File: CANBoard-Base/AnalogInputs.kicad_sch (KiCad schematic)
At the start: 26 parts, among them U2 LM324, U3 LM324, U4 SRV05-4

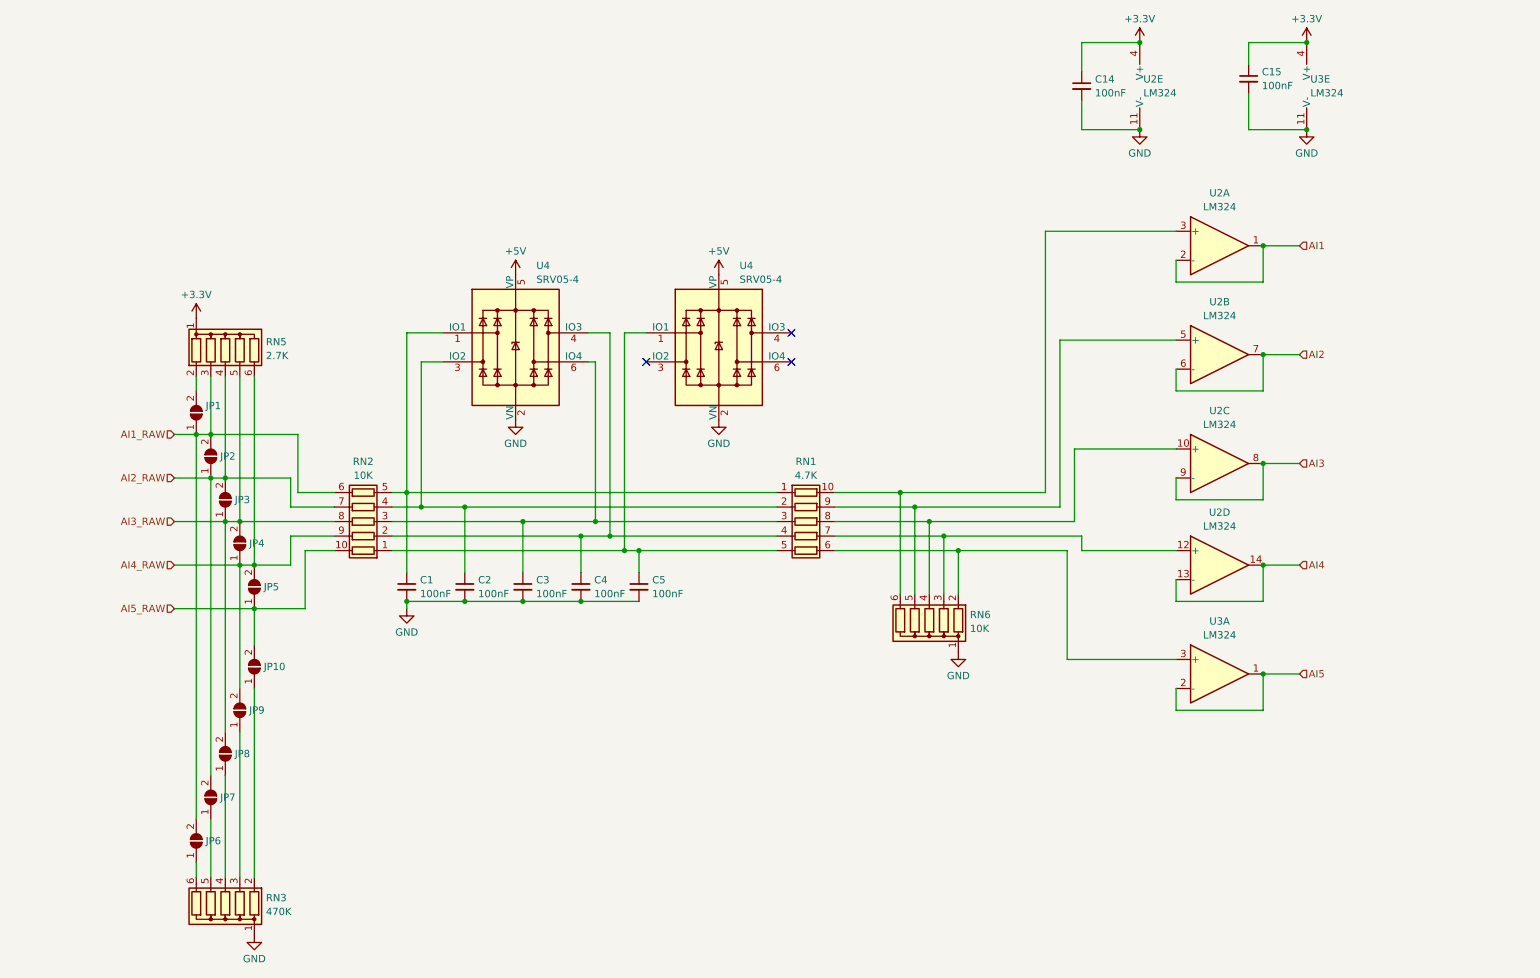
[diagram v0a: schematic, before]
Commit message: Switched to v2
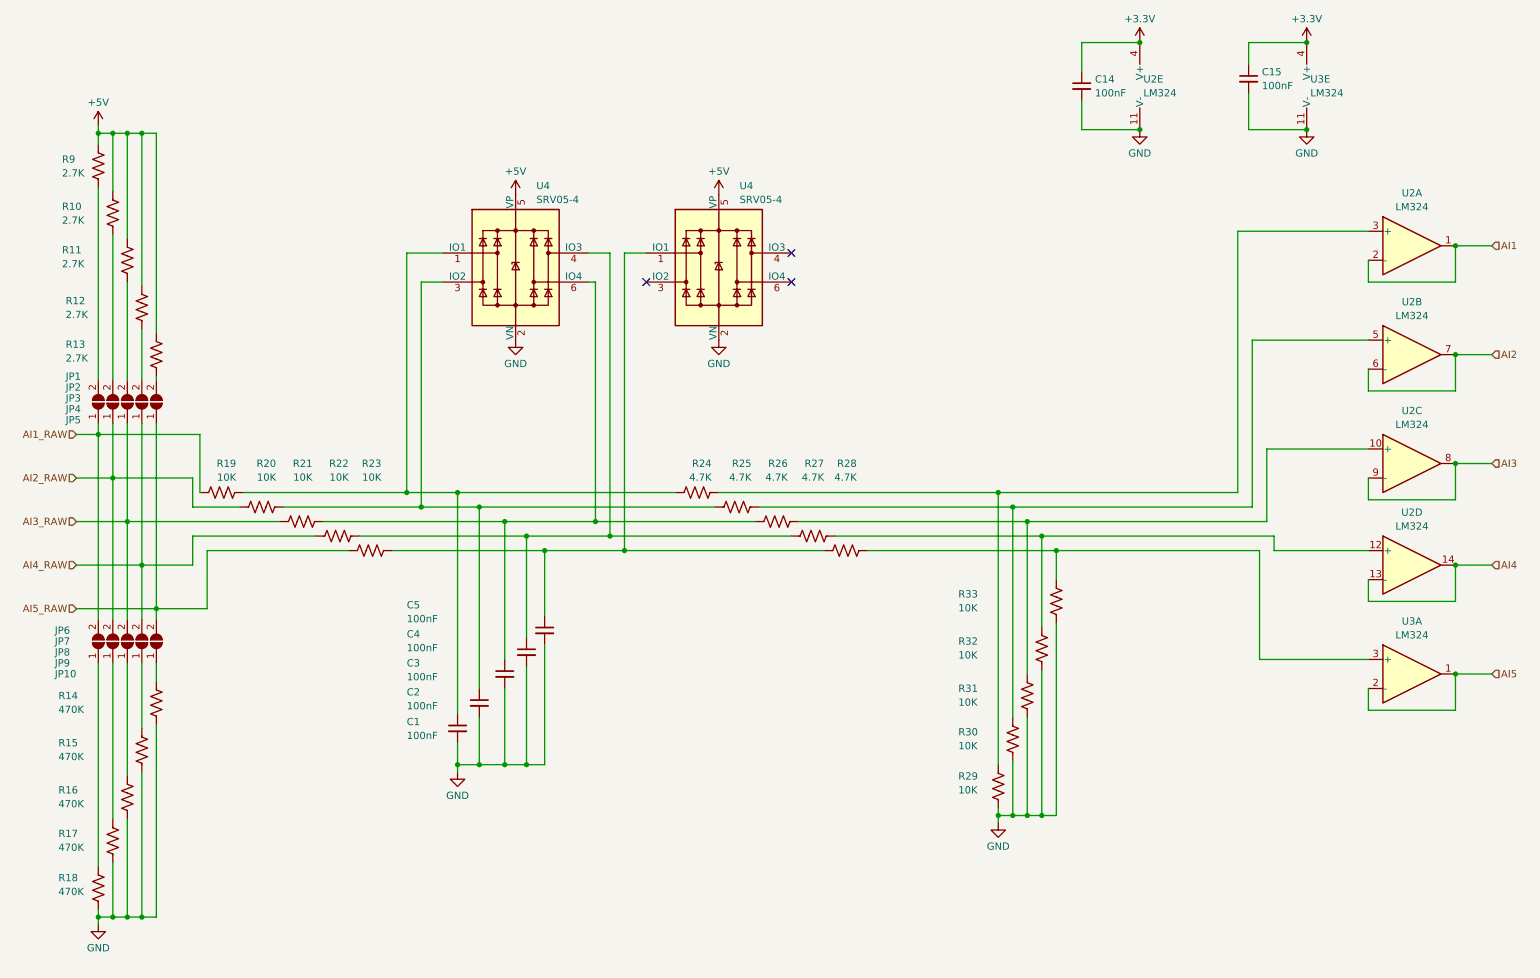
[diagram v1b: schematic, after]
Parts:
- removed RN1: 4.7K, symbol Device:R_Pack05
- removed RN2: 10K, symbol Device:R_Pack05
- removed RN3: 470K, Resistor_THT:R_Array_SIP6, symbol Device:R_Network05
- removed RN5: 2.7K, Resistor_THT:R_Array_SIP6, symbol Device:R_Network05
- removed RN6: 10K, Resistor_THT:R_Array_SIP6, symbol Device:R_Network05
- added R10, R11, R12, R13, R9: 2.7K, Resistor_SMD:R_0805_2012Metric, symbol Device:R_US
- added R14, R15, R16, R17, R18: 470K, Resistor_SMD:R_0805_2012Metric, symbol Device:R_US
- added R19, R20, R21, R22, R23, R29, R30, R31, R32, R33: 10K, Resistor_SMD:R_0805_2012Metric, symbol Device:R_US
- added R24, R25, R26, R27, R28: 4.7K, Resistor_SMD:R_0805_2012Metric, symbol Device:R_US
- JP1, JP10, JP2, JP3, JP4, JP5, JP6, JP7, JP8, JP9: footprint (none) -> Jumper:SolderJumper-2_P1.3mm_Open_RoundedPad1.0x1.5mm
- U2, U3: footprint (none) -> Package_SO:TSSOP-14_4.4x5mm_P0.65mm
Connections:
- net +5V: now also R10.1, R11.1, R12.1, R13.1, R9.1
- net AI1_RAW: now also R19.1; no longer JP2.2 (B)
- net AI2_RAW: now also R20.1; no longer JP3.2 (B)
- net AI3_RAW: now also R21.1; no longer JP4.2 (B)
- net AI4_RAW: now also R22.1; no longer JP5.2 (B)
- net AI5_RAW: now also R23.1
- net GND: now also R14.2, R15.2, R16.2, R17.2, R18.2, R29.2, R30.2, R31.2, R32.2, R33.2
- net at JP8.1 (A): now also R16.1
- net at JP9.1 (A): now also R15.1
- net at U2.10 (+): now also R26.2, R31.1
- net at JP1.2 (B): now also R9.2
- net at JP10.1 (A): now also R14.1
- net at JP7.1 (A): now also R17.1
- net at JP6.1 (A): now also R18.1
- net at C3.1, U4.6 (IO4): now also R21.2, R26.1
- net at U2.5 (+): now also R25.2, R30.1
- net at C1.1, U4.1 (IO1): now also R19.2, R24.1
- net at C2.1, U4.3 (IO2): now also R20.2, R25.1
- net at C4.1, U4.4 (IO3): now also R22.2, R27.1
- net at C5.1, U4.1 (IO1): now also R23.2, R28.1
- net at U2.3 (+): now also R24.2, R29.1
- net at U3.3 (+): now also R28.2, R33.1
- net at U2.12 (+): now also R27.2, R32.1
- new net: JP4.2 (B), R12.2
- new net: JP5.2 (B), R13.2
- new net: JP2.2 (B), R10.2
- new net: JP3.2 (B), R11.2
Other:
- moved on the sheet: C1, C2, C3, C4, C5, JP1, JP10, JP2, JP3, JP4, JP5, JP6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

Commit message: Update to Kicad 8
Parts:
- renumbered U4 to U5

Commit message: first layout complete
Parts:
- renumbered U2 to U3
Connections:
- net AI1: now also U2.8, U2.9 (-); no longer U2.1, U2.2 (-)
- net AI3: now also U2.1, U2.2 (-); no longer U2.8, U2.9 (-)
- net AI4: now also U3.6 (-), U3.7; no longer U3.13 (-), U3.14
- net at R24.2, R29.1: now also U2.10 (+); no longer U2.3 (+)
- net at R26.2, R31.1: now also U2.3 (+); no longer U2.10 (+)
- net at C3.1, R21.2, R26.1: now also U4.4 (IO3); no longer U4.6 (IO4)
- net at C4.1, R22.2, R27.1: now also U5.1 (IO1); no longer U4.4 (IO3)
- net at R27.2, R32.1: now also U3.5 (+); no longer U3.12 (+)
- net at C5.1, R23.2, R28.1: now also U5.3 (IO2); no longer U5.1 (IO1)

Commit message: as built v1
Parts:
- C1, C14, C15, C2, C3, C4, C5: JLC_PN (none) -> C49678
- JP1, JP10, JP2, JP3, JP4, JP5, JP6, JP7, JP8, JP9: now left out of the parts list
- R10, R11, R12, R13, R9: JLC_PN (none) -> C17530
- R14, R15, R16, R17, R18: JLC_PN (none) -> C17709
- R19, R20, R21, R22, R23, R29, R30, R31, R32, R33: JLC_PN (none) -> C17414
- R24, R25, R26, R27, R28: JLC_PN (none) -> C17673
- U2, U3: JLC_PN (none) -> C7942
- U4, U5: JLC_PN (none) -> C384887

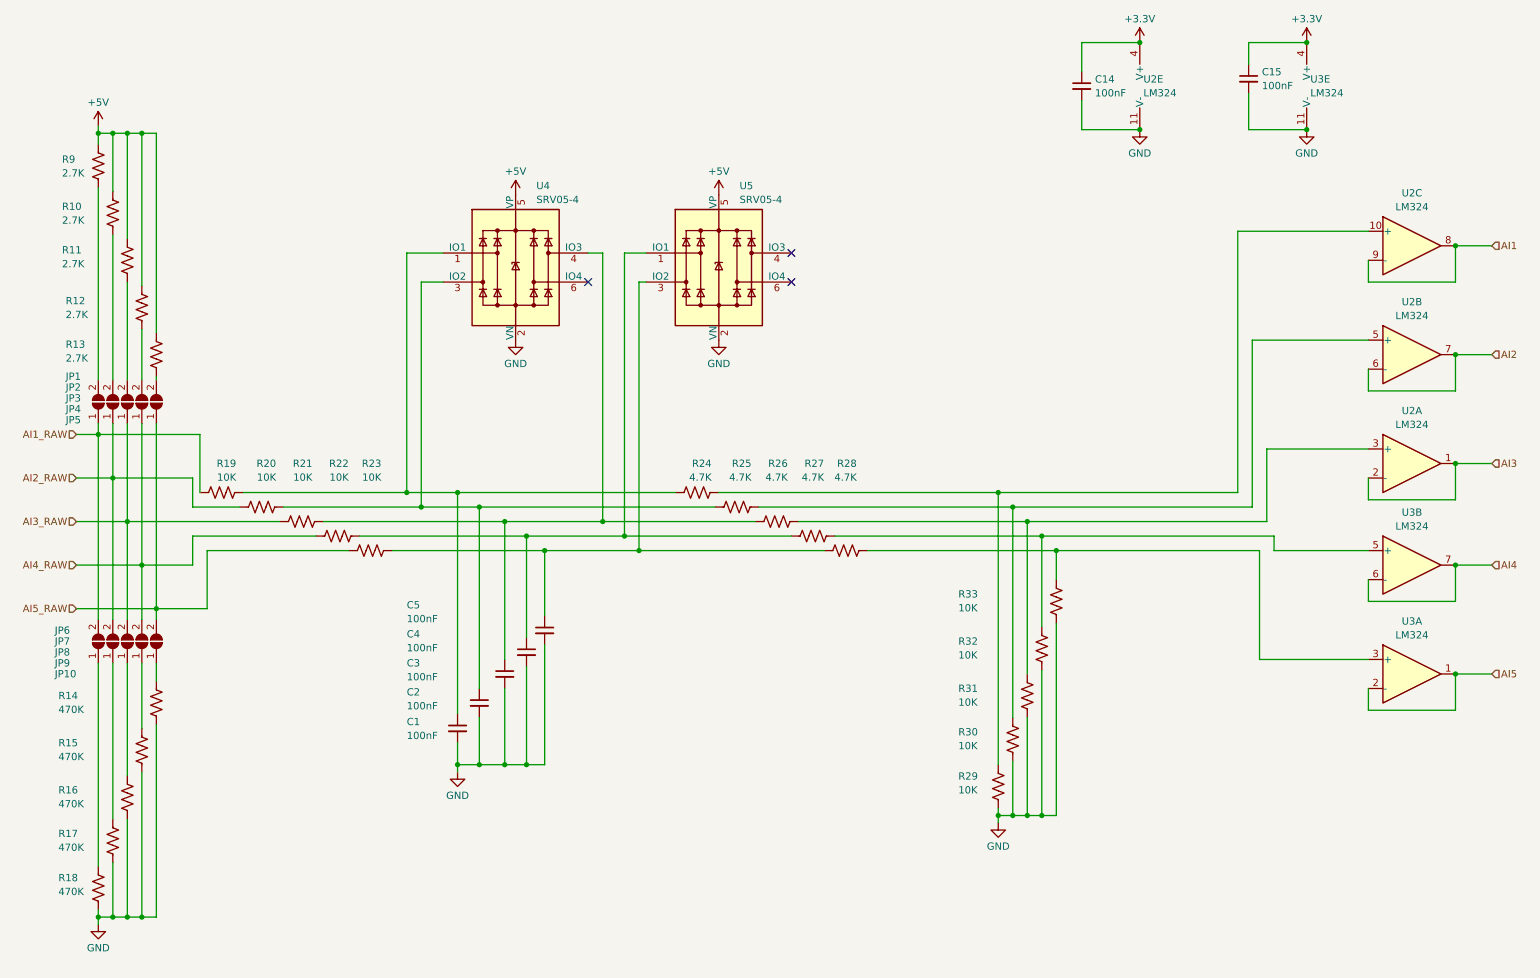
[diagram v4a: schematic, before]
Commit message: moved dtm connectors together
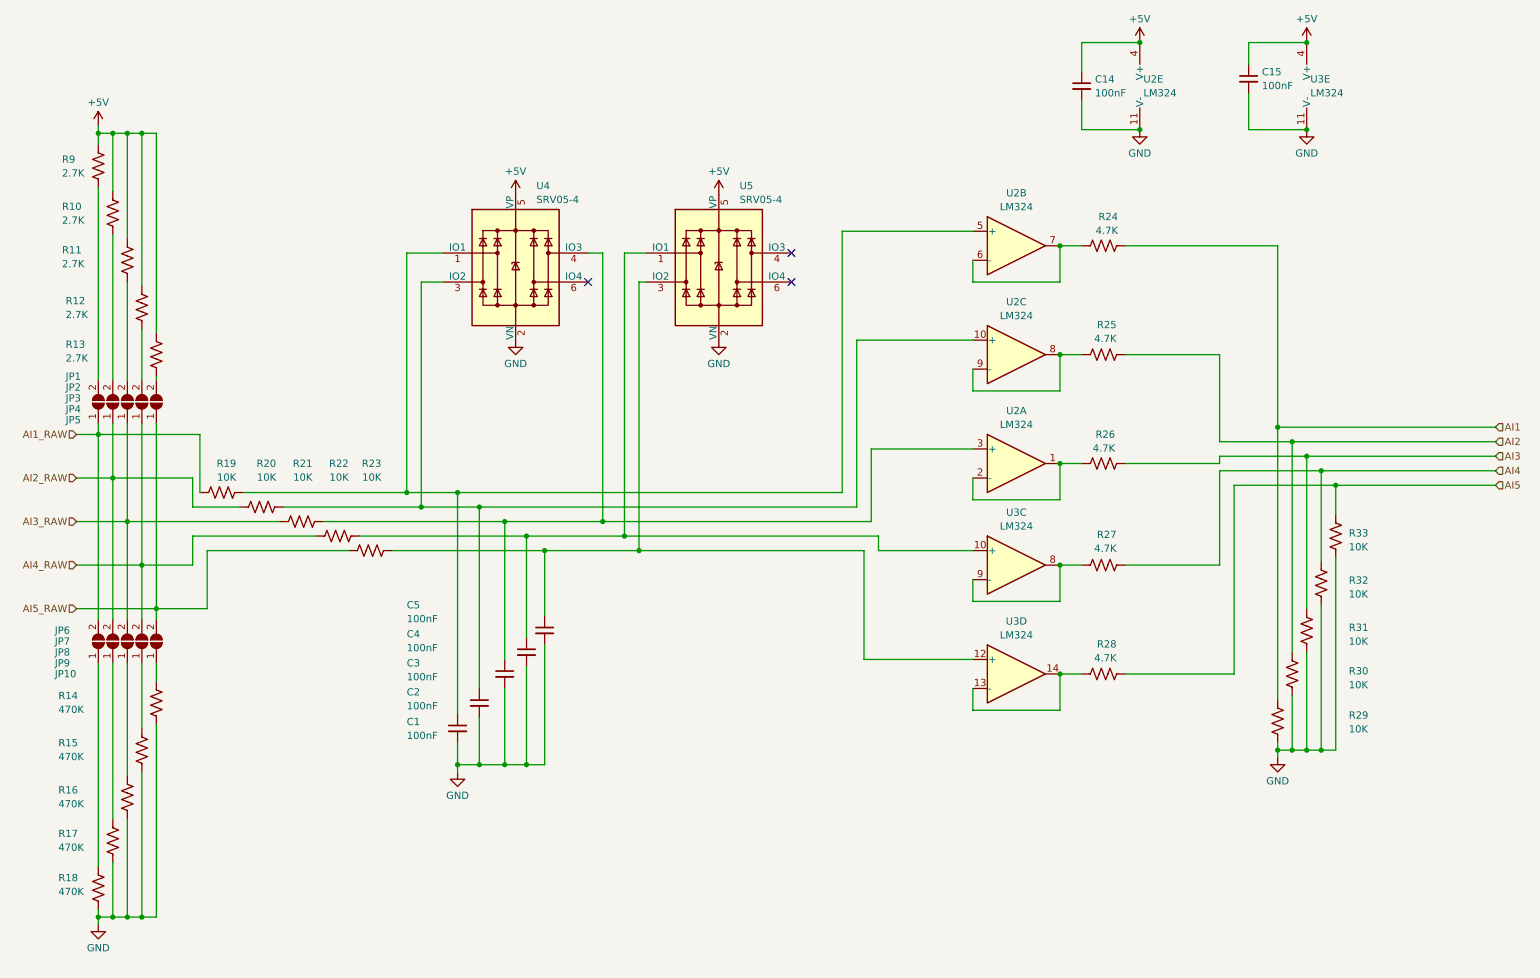
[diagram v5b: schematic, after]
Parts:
- R14, R15, R16, R17, R18: JLC_PN C17709 -> C17530
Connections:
- net +3.3V is gone; now on net +5V: C14.1, C15.1, U2.4 (V+), U3.4 (V+)
- net AI1: now also R24.2, R29.1; no longer U2.8, U2.9 (-)
- net AI2: now also R25.2, R30.1; no longer U2.6 (-), U2.7
- net AI3: now also R26.2, R31.1; no longer U2.1, U2.2 (-)
- net AI4: now also R27.2, R32.1; no longer U3.6 (-), U3.7
- net AI5: now also R28.2, R33.1; no longer U3.1, U3.2 (-)
- net at C3.1, R21.2, U4.4 (IO3): now also U2.3 (+); no longer R26.1
- net at C1.1, R19.2, U4.1 (IO1): now also U2.5 (+); no longer R24.1
- net at C2.1, R20.2, U4.3 (IO2): now also U2.10 (+); no longer R25.1
- net at C4.1, R22.2, U5.1 (IO1): now also U3.10 (+); no longer R27.1
- net at C5.1, R23.2, U5.3 (IO2): now also U3.12 (+); no longer R28.1
- new net: R26.1, U2.1, U2.2 (-)
- new net: R25.1, U2.8, U2.9 (-)
- new net: R27.1, U3.8, U3.9 (-)
- new net: R24.1, U2.6 (-), U2.7
- new net: R28.1, U3.13 (-), U3.14
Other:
- moved on the sheet: R24, R25, R26, R27, R28, R29, R30, R31, R32, R33, U2A, U2B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

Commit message: version 1.1 ready for manuf
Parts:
- R14, R15, R16, R17, R18: JLC_PN C17530 -> C17709
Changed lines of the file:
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@@
 	(title_block
 		(title "CANBoard-Base")
-		(date "2024-07-13")
-		(rev "v1")
+		(date "2025-01-17")
+		(rev "v1.1")
 		(company "Dingo Electronics")
 		(comment 1 "github.com/corygrant")
@@
 			)
 		)
-		(property "JLC_PN" "C17530"
+		(property "JLC_PN" "C17709"
 			(at 38.735 144.145 0)
 			(effects
@@
 			)
 		)
-		(property "JLC_PN" "C17530"
+		(property "JLC_PN" "C17709"
 			(at 33.655 160.02 0)
 			(effects
@@
 			)
 		)
-		(property "JLC_PN" "C17530"
+		(property "JLC_PN" "C17709"
 			(at 36.195 152.4 0)
 			(effects
@@
 			)
 		)
-		(property "JLC_PN" "C17530"
+		(property "JLC_PN" "C17709"
 			(at 31.115 168.275 0)
 			(effects
@@
 			)
 		)
-		(property "JLC_PN" "C17530"
+		(property "JLC_PN" "C17709"
 			(at 41.275 135.89 0)
 			(effects
